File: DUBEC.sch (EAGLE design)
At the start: 51 parts

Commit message: Spec inductor
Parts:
- added U$1, U$2: H1, dubec:H1
- 12L: device dubec:I10UH -> dubec:IWE-HCI_10UH
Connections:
- net 5V: now also U$2.1
- net GND: now also U$1.1
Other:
- moved on the sheet: 5COUT, 5CVCC, 5L, 5R1, 5R2, DZDIV, RI1

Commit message: Optimized voltage divider resistors
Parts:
- 12RT: value 35.7kOhm -> RES48.7K_20; device dubec:RES35.7K_20 -> dubec:RES48.7K_20
- 5RT: value 18.2kOhm -> RES41.2K_20
- RDIV1: value 243kOhm -> RES26.1K_20; device dubec:RES243K_20 -> dubec:RES26.1K_20
- RDIV2: value 40.2kOhm -> RES4.42K_20; device dubec:RES40.2K_20 -> dubec:RES4.42K_20
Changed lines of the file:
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@@
 <part name="12L" library="dubec" deviceset="I" device="WE-HCI_10UH" value="10uH"/>
 <part name="12C1" library="dubec" deviceset="CAP" device="4.7UF_6.3V" value="4.7uF"/>
-<part name="12RT" library="dubec" deviceset="RES" device="35.7K_20" value="35.7kOhm"/>
+<part name="12RT" library="dubec" deviceset="RES" device="48.7K_20" value="RES48.7K_20"/>
 <part name="12RBOT" library="dubec" deviceset="RES" device="90.9K_20" value="90.9kOhm"/>
 <part name="12RFF" library="dubec" deviceset="RES" device="10K_20" value="10kOhm"/>
@@
 <part name="5R1" library="dubec" deviceset="RES" device="1M_20" value="1MOhm"/>
 <part name="5CSS" library="dubec" deviceset="CAP" device="10NF_10V" value="10nF"/>
-<part name="5RT" library="dubec" deviceset="RES" device="41.2K_20" value="18.2kOhm"/>
+<part name="5RT" library="dubec" deviceset="RES" device="41.2K_20" value="RES41.2K_20"/>
 <part name="GND1" library="supply1" deviceset="GND" device=""/>
 <part name="35V_NO" library="supply1" deviceset="V+" device=""/>
@@
 <part name="DFB" library="dubec" deviceset="D_SCH" device="30V_0.2A" value="D_SCH30V_0.2A"/>
 <part name="12D" library="dubec" deviceset="D_SCH" device="30V_0.2A"/>
-<part name="RDIV1" library="dubec" deviceset="RES" device="243K_20" value="243kOhm"/>
-<part name="RDIV2" library="dubec" deviceset="RES" device="40.2K_20" value="40.2kOhm"/>
+<part name="RDIV1" library="dubec" deviceset="RES" device="26.1K_20" value="RES26.1K_20"/>
+<part name="RDIV2" library="dubec" deviceset="RES" device="4.42K_20" value="RES4.42K_20"/>
 <part name="DZDIV" library="dubec" deviceset="D_ZENER" device="5.1V" value="5.1V"/>
 <part name="5COUT" library="dubec" deviceset="CAP" device="47UF_6.3V" value="47uF"/>

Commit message: Cleanup
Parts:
- 12CB1: device dubec:CAP0.1UF_35V -> dubec:CAP0.1UF_50V
- 12CB2: device dubec:CAP0.1UF_35V -> dubec:CAP0.1UF_25V
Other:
- moved on the sheet: 12C1, 12CFF, 12D, 12LED, 12RLED, 5D, DISP, DUPS

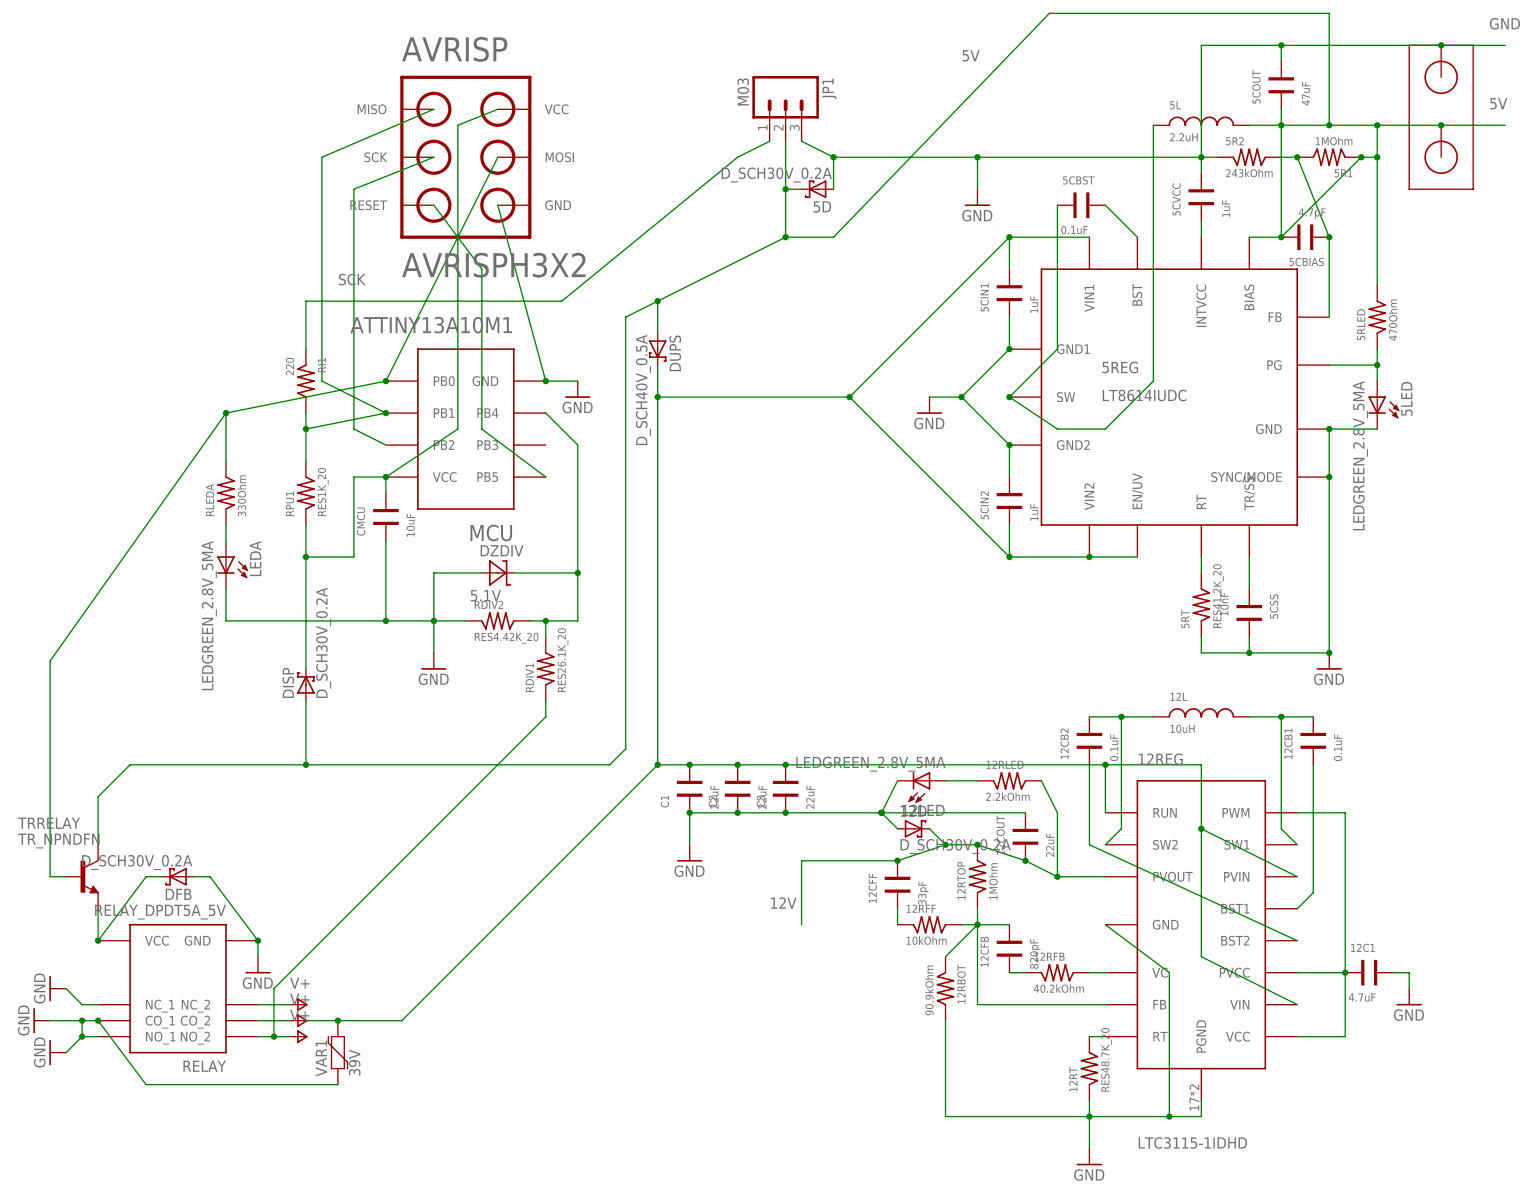
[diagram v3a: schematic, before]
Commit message: Problematic relay downgrade to 2A due to non-stock
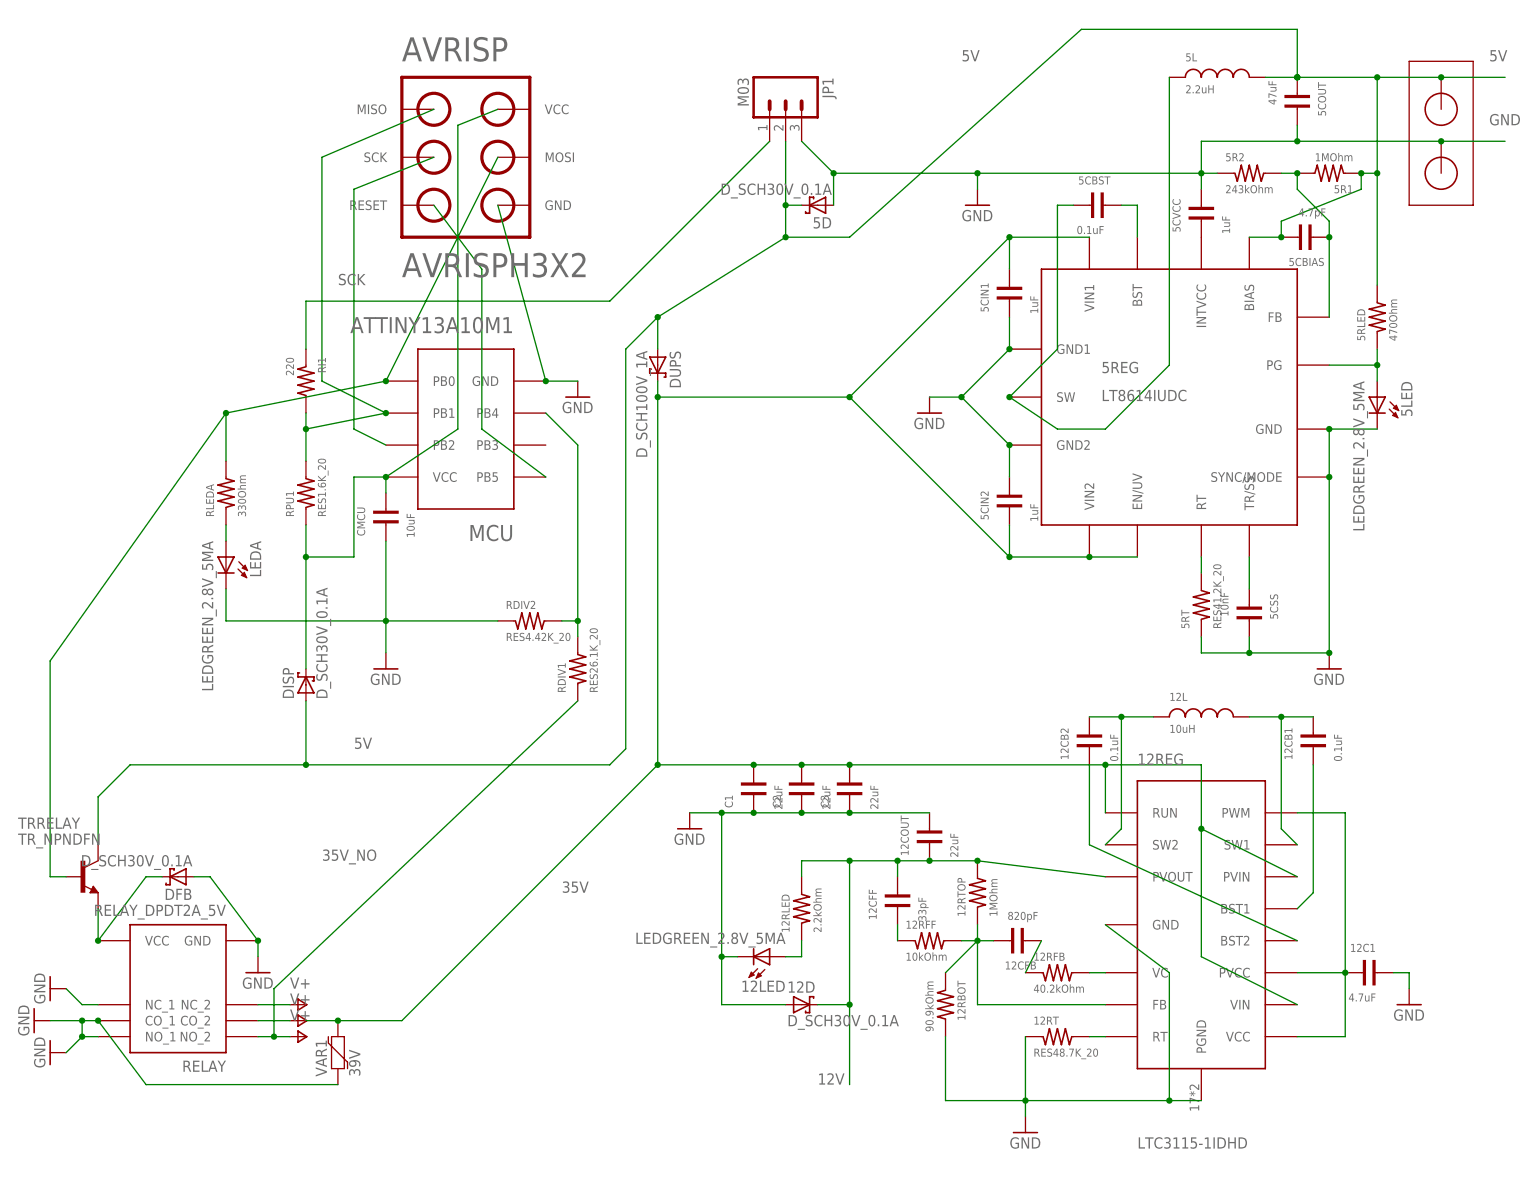
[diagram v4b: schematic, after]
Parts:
- removed DZDIV: 5.1V, dubec:D_ZENER5.1V
- 12CB2: device dubec:CAP0.1UF_25V -> dubec:CAP0.1UF_50V
- 12D, 5D, DFB, DISP: value D_SCH30V_0.2A -> D_SCH30V_0.1A; device dubec:D_SCH30V_0.2A -> dubec:D_SCH30V_0.1A
- 5COUT: device dubec:CAP47UF_6.3V -> dubec:CAP47UF_6.3V-12
- DUPS: value D_SCH40V_0.5A -> D_SCH100V_1A; device dubec:D_SCH40V_0.5A -> dubec:D_SCH100V_1A
- RELAY: value RELAY_DPDT5A_5V -> RELAY_DPDT2A_5V; device dubec:RELAY_DPDT5A_5V -> dubec:RELAY_DPDT2A_5V
- RPU1: value RES1K_20 -> RES1.6K_20; device dubec:RES1K_20 -> dubec:RES1.6K_20
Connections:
- net GND: no longer DZDIV.A
- net VDIV: no longer DZDIV.C
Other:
- moved on the sheet: 12D, 12LED, 5D, 5L, DUPS

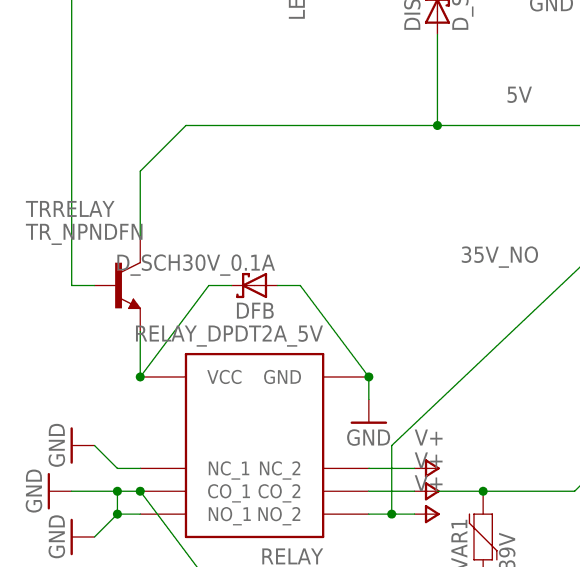
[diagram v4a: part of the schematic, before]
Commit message: Revert to gullwing, incomplete
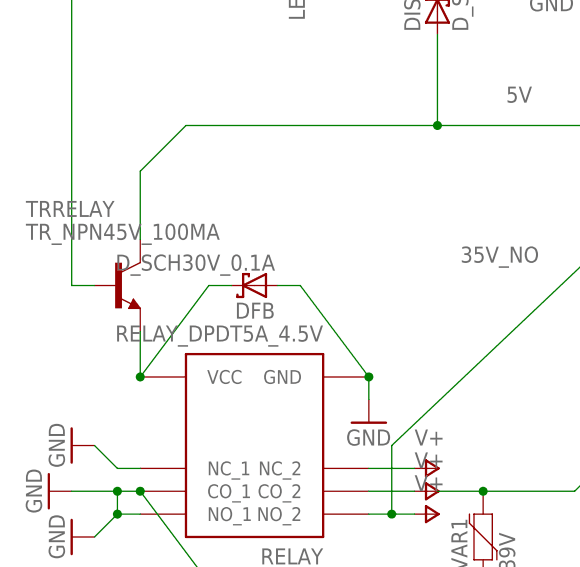
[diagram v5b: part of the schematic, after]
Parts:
- RELAY: value RELAY_DPDT2A_5V -> RELAY_DPDT5A_4.5V; device dubec:RELAY_DPDT2A_5V -> dubec:RELAY_DPDT5A_4.5V
- TRRELAY: value TR_NPNDFN -> TR_NPN45V_100MA; device dubec:TR_NPNDFN -> dubec:TR_NPN45V_100MA
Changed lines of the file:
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@@
 <part name="5REG" library="dubec" deviceset="LT8614" device="IUDC" value="LT8614IUDC"/>
 <part name="MCU" library="dubec" deviceset="ATTINY13A" device="10M1"/>
-<part name="RELAY" library="dubec" deviceset="RELAY_DPDT" device="2A_5V" value="RELAY_DPDT2A_5V"/>
+<part name="RELAY" library="dubec" deviceset="RELAY_DPDT" device="5A_4.5V" value="RELAY_DPDT5A_4.5V"/>
 <part name="12REG" library="dubec" deviceset="LTC3115-1" device="IDHD" value="LTC3115-1IDHD"/>
 <part name="C1" library="dubec" deviceset="CAP" device="22UF_35V" value="22uF"/>
@@
 <part name="AVRISP" library="dubec" deviceset="AVRISP" device="H3X2" value="AVRISPH3X2"/>
 <part name="DISP" library="dubec" deviceset="D_SCH" device="30V_0.1A" value="D_SCH30V_0.1A"/>
-<part name="TRRELAY" library="dubec" deviceset="TR_NPN" device="DFN" value="TR_NPNDFN"/>
+<part name="TRRELAY" library="dubec" deviceset="TR_NPN" device="45V_100MA" value="TR_NPN45V_100MA"/>
 <part name="DFB" library="dubec" deviceset="D_SCH" device="30V_0.1A" value="D_SCH30V_0.1A"/>
 <part name="12D" library="dubec" deviceset="D_SCH" device="30V_0.1A" value="D_SCH30V_0.1A"/>

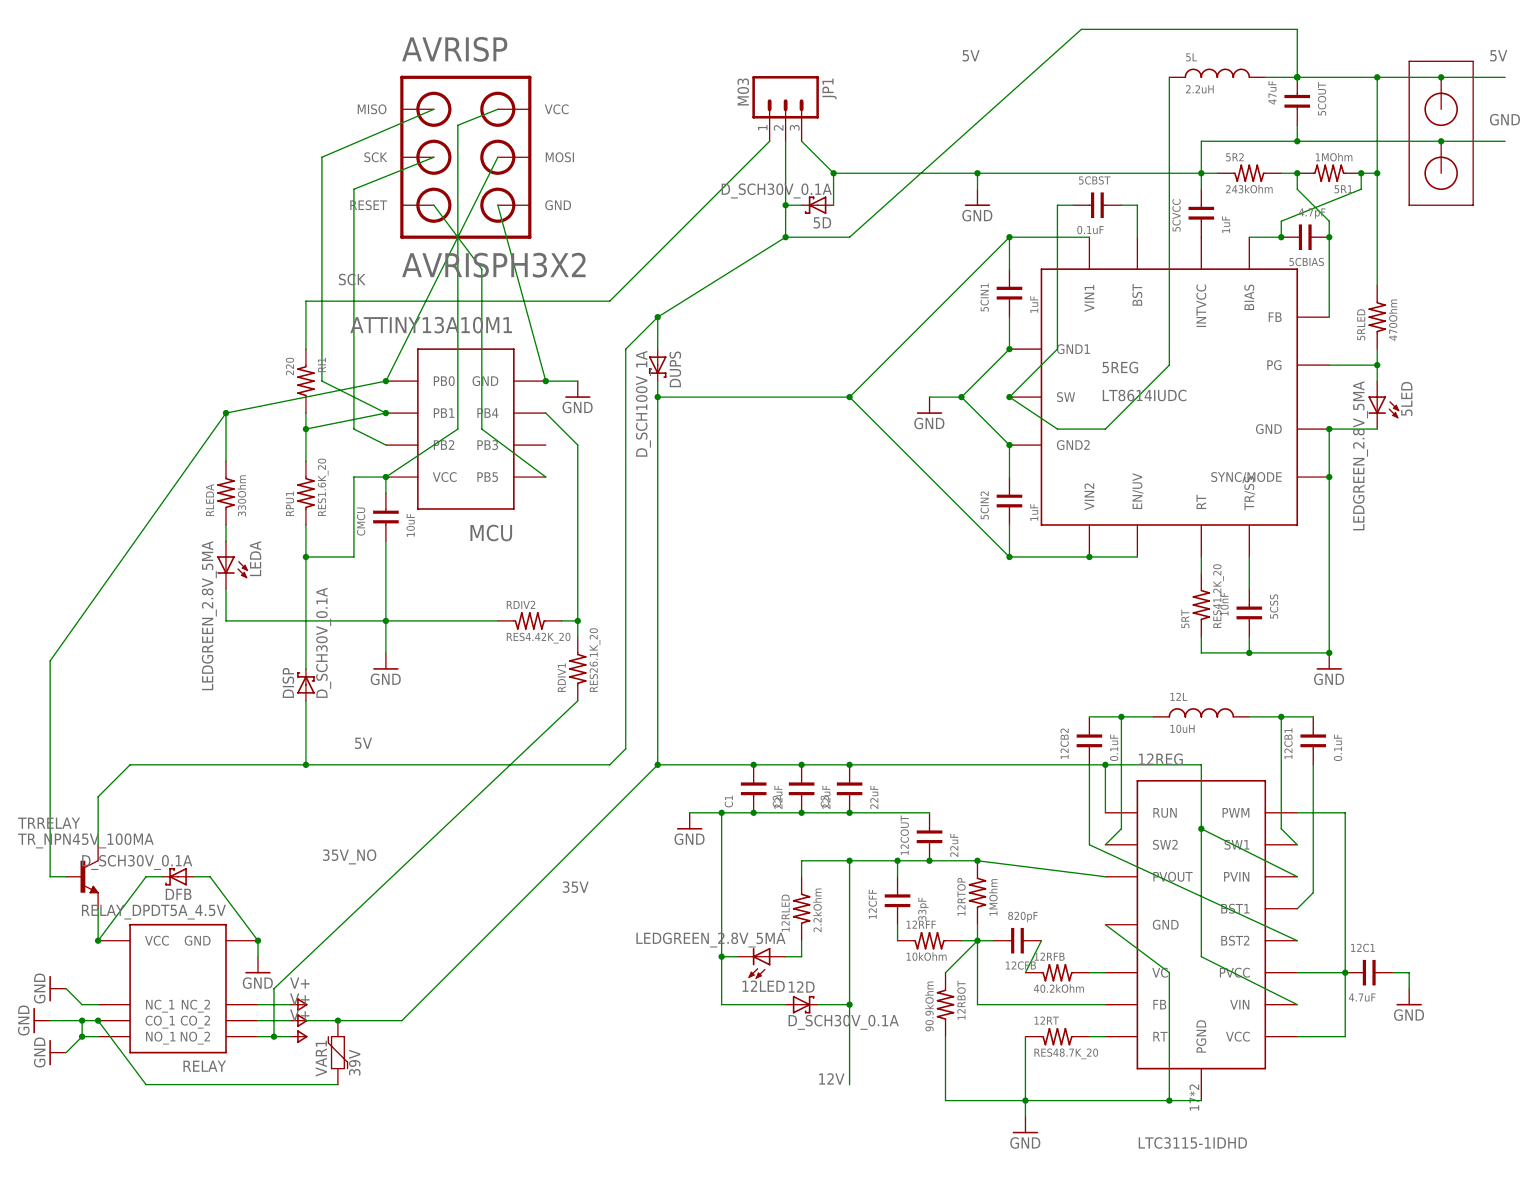
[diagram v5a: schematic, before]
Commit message: Alum cap instead of super cap
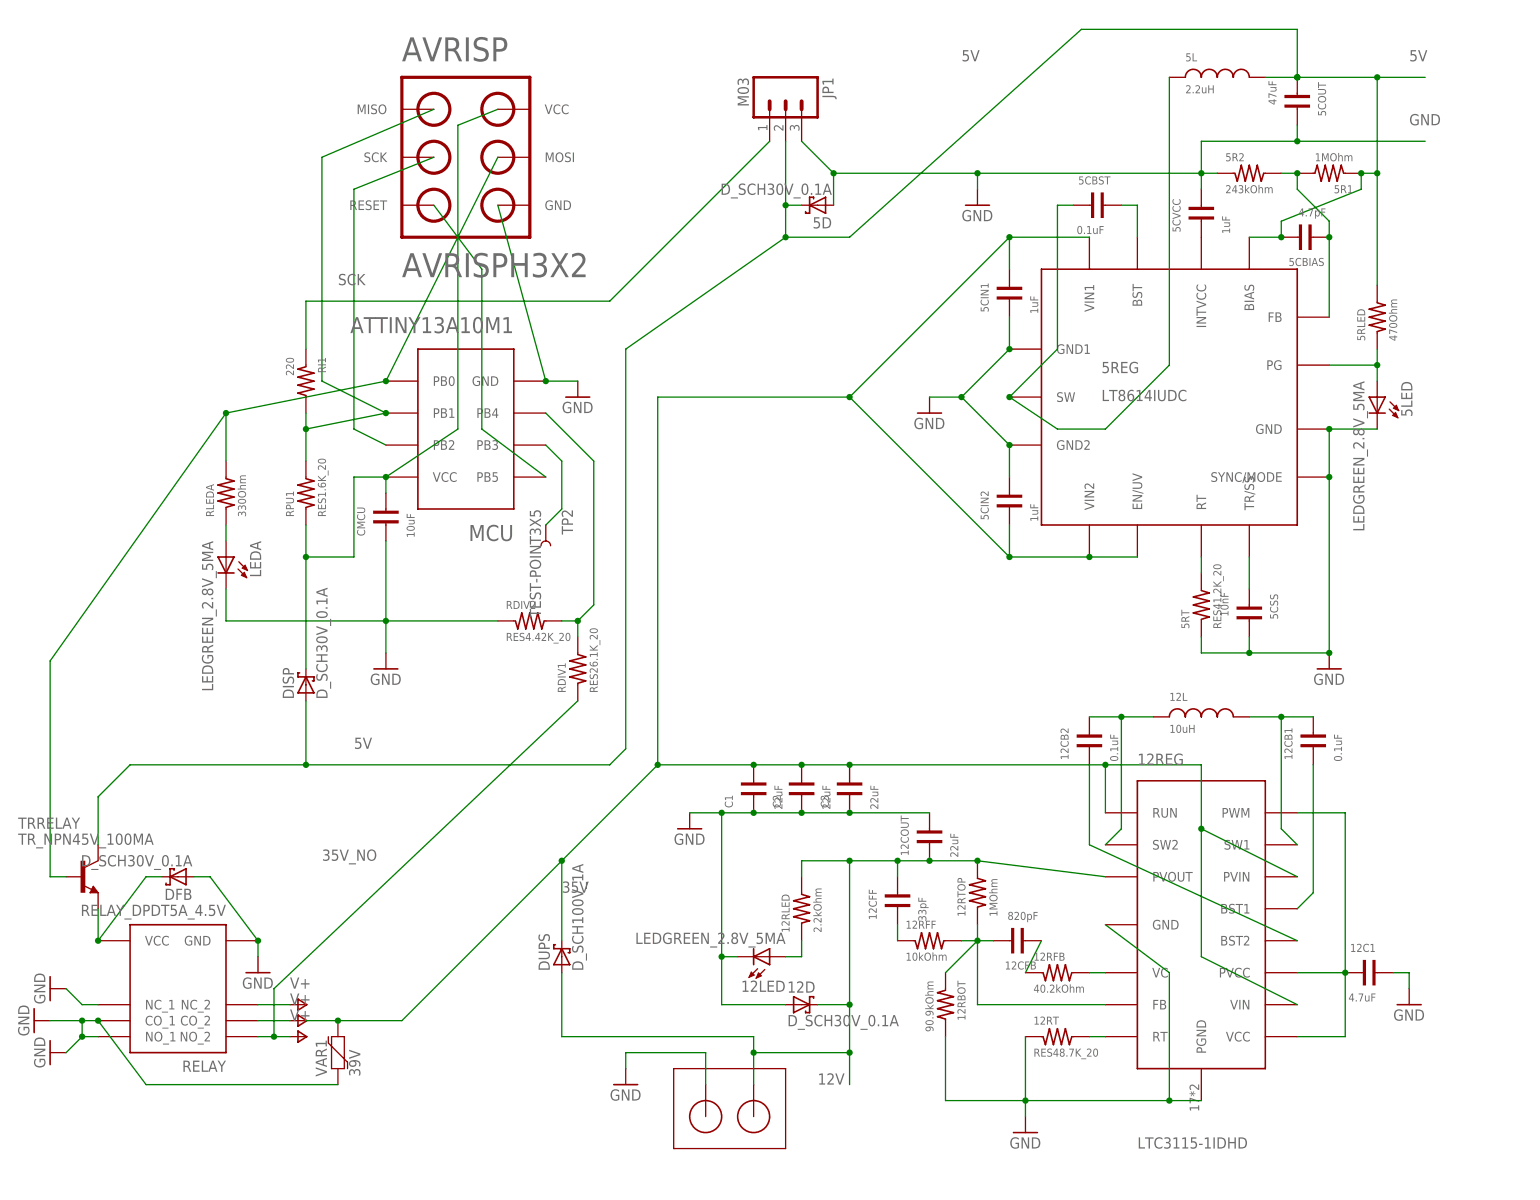
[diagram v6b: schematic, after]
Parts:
- removed U$1, U$2: H1, dubec:H1
- added TP2: TEST-POINT3X5, SparkFun-Passives:TEST-POINT3X5
- added U$3, U$4: H1, dubec:H1
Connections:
- new net N$2: MCU.PB3, TP2.1
- net 12V: now also DUPS.A, U$3.1
- net 5V: no longer DUPS.A, U$2.1
- net GND: now also U$4.1; no longer U$1.1
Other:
- moved on the sheet: DUPS

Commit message: Tweaks
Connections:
- net 5V_RAW renamed 5V_SW
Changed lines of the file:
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@@
 </segment>
 </net>
-<net name="5V_RAW" class="0">
+<net name="5V_SW" class="0">
 <segment>
 <pinref part="5REG" gate="G$1" pin="SW"/>
